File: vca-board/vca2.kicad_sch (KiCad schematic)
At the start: 8 parts, among them U1 SSI2164-Split, U4 TL074

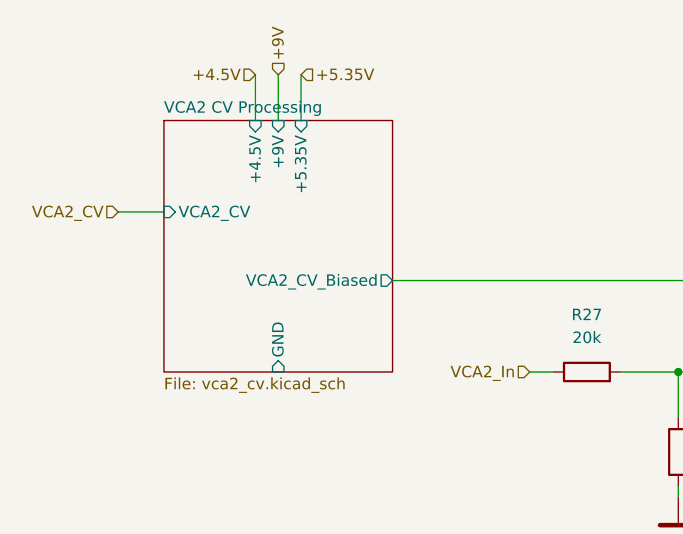
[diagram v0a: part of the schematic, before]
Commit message: VCA components linked
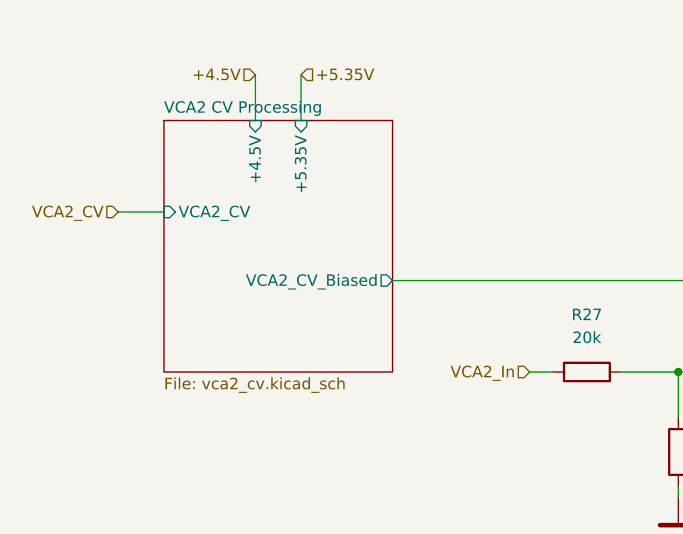
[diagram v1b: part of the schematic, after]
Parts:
- C11: footprint (none) -> Capacitor_SMD:C_0603_1608Metric_Pad1.08x0.95mm_HandSolder; LCSC (none) -> C3012379
- C12: footprint (none) -> Capacitor_SMD:C_0603_1608Metric_Pad1.08x0.95mm_HandSolder; LCSC (none) -> C160903
- R27, R29: LCSC (none) -> C4184
- R28: LCSC (none) -> C22962
- R30: LCSC (none) -> C21190
- U4: footprint (none) -> Package_SO:SOIC-14_3.9x8.7mm_P1.27mm; LCSC (none) -> C6963
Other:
- sheet VCA2 CV Processing ports: added none; removed +9V, GND
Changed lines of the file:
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@@
-    (stroke (width 0) (type default) (color 0 0 0 0))
-  )
-  (wire (pts (xy 63.5 43.18) (xy 63.5 48.26))
     (stroke (width 0) (type default) (color 0 0 0 0))
   )
@@
     (effects (font (size 1.27 1.27)) (justify left))
   )
-  (hierarchical_label "+9V" (shape input) (at 63.5 43.18 90)
-    (effects (font (size 1.27 1.27)) (justify left))
-  )
   (symbol (lib_id "Amplifier_Operational:TL074") (at 146.05 78.74 0) (mirror x) (unit 3)
     (in_bom yes) (on_board yes) (fields_autoplaced)
     (property "Reference" "U4" (id 0) (at 146.05 68.58 0))
     (property "Value" "TL074" (id 1) (at 146.05 71.12 0))
-    (property "Footprint" "" (id 2) (at 144.78 81.28 0)
+    (property "Footprint" "Package_SO:SOIC-14_3.9x8.7mm_P1.27mm" (id 2) (at 144.78 81.28 0)
       (effects (font (size 1.27 1.27)) hide)
     )
     (property "Datasheet" "http://www.ti.com/lit/ds/symlink/tl071.pdf" (id 3) (at 147.32 83.82 0)
+      (effects (font (size 1.27 1.27)) hide)
+    )
+    (property "LCSC" "C6963" (id 4) (at 146.05 78.74 0)
       (effects (font (size 1.27 1.27)) hide)
     )
@@
     (property "Reference" "C12" (id 0) (at 146.05 46.99 90))
     (property "Value" "100p" (id 1) (at 146.05 49.53 90))
-    (property "Footprint" "" (id 2) (at 142.24 55.5752 0)
+    (property "Footprint" "Capacitor_SMD:C_0603_1608Metric_Pad1.08x0.95mm_HandSolder" (id 2) (at 142.24 55.5752 0)
       (effects (font (size 1.27 1.27)) hide)
     )
     (property "Datasheet" "~" (id 3) (at 146.05 54.61 0)
+      (effects (font (size 1.27 1.27)) hide)
+    )
+    (property "LCSC" "C160903" (id 4) (at 146.05 54.61 0)
       (effects (font (size 1.27 1.27)) hide)
     )
@@
     )
     (property "Datasheet" "~" (id 3) (at 97.79 76.2 0)
+      (effects (font (size 1.27 1.27)) hide)
+    )
+    (property "LCSC" "C4184" (id 4) (at 97.79 76.2 0)
       (effects (font (size 1.27 1.27)) hide)
     )
@@
       (effects (font (size 1.27 1.27)) hide)
     )
+    (property "LCSC" "C4184" (id 4) (at 146.05 66.04 0)
+      (effects (font (size 1.27 1.27)) hide)
+    )
     (pin "1")
     (pin "2")
@@
       (effects (font (size 1.27 1.27)) (justify right))
     )
-    (property "Footprint" "" (id 2) (at 106.9848 90.17 0)
+    (property "Footprint" "Capacitor_SMD:C_0603_1608Metric_Pad1.08x0.95mm_HandSolder" (id 2) (at 106.9848 90.17 0)
       (effects (font (size 1.27 1.27)) hide)
     )
     (property "Datasheet" "~" (id 3) (at 107.95 93.98 0)
+      (effects (font (size 1.27 1.27)) hide)
+    )
+    (property "LCSC" "C3012379" (id 4) (at 107.95 93.98 0)
       (effects (font (size 1.27 1.27)) hide)
     )
@@
       (effects (font (size 1.27 1.27)) hide)
     )
+    (property "LCSC" "C21190" (id 4) (at 162.56 78.74 0)
+      (effects (font (size 1.27 1.27)) hide)
+    )
     (pin "1")
     (pin "2")
@@
     )
     (property "Datasheet" "~" (id 3) (at 107.95 85.09 0)
+      (effects (font (size 1.27 1.27)) hide)
+    )
+    (property "LCSC" "C22962" (id 4) (at 107.95 85.09 0)
       (effects (font (size 1.27 1.27)) hide)
     )
@@
       (effects (font (size 1.27 1.27)) (justify left top))
     )
-    (pin "GND" input (at 63.5 76.2 270)
-      (effects (font (size 1.27 1.27)) (justify left))
-    )
-    (pin "+9V" input (at 63.5 48.26 90)
-      (effects (font (size 1.27 1.27)) (justify right))
-    )
     (pin "VCA2_CV" input (at 50.8 58.42 180)

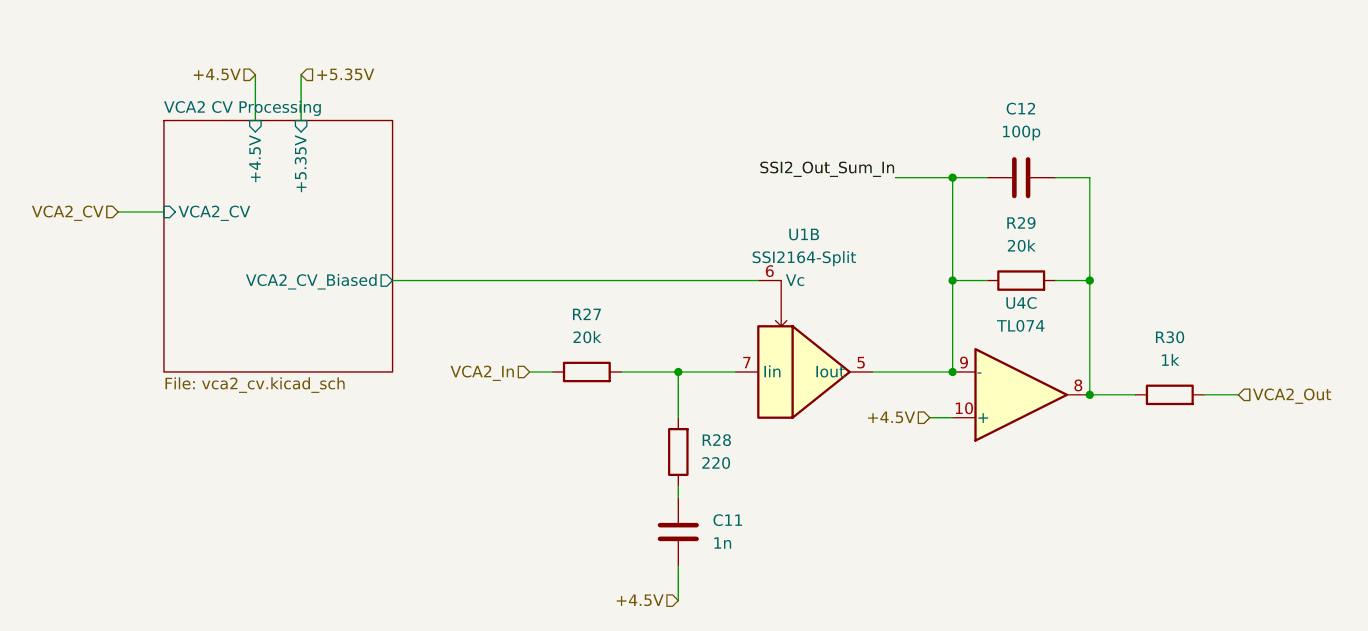
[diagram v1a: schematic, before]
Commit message: VCA board components placed
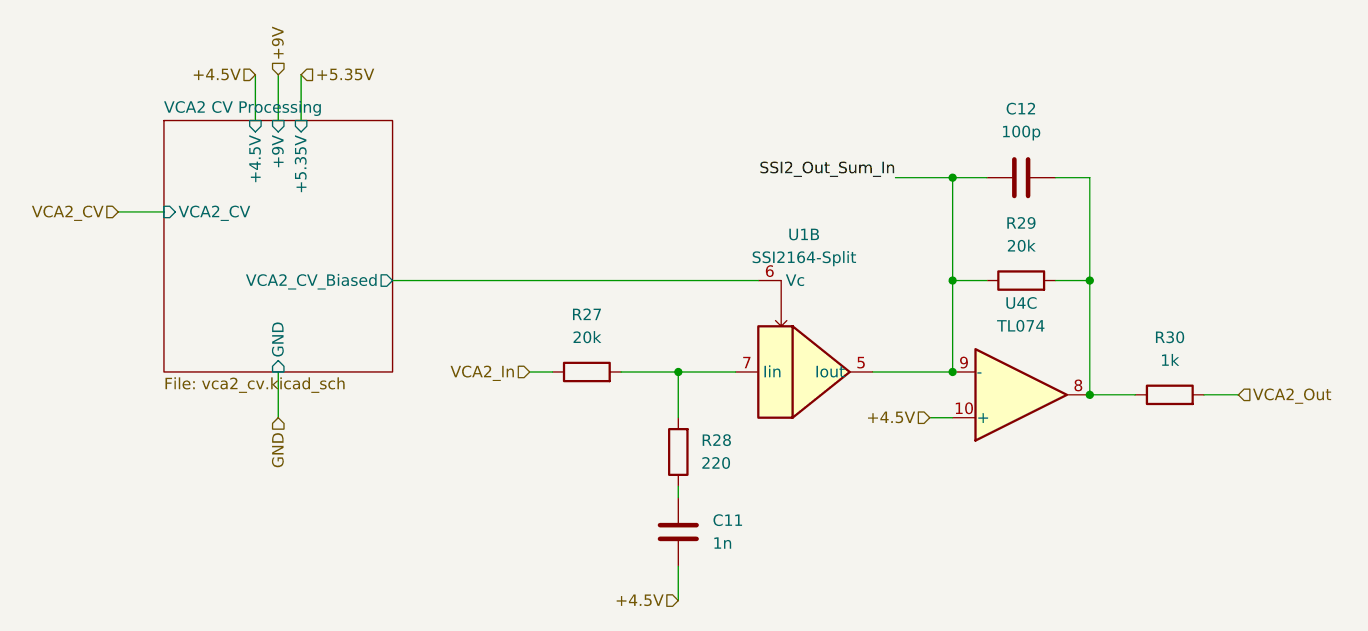
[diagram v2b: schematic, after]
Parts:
- R27, R28, R29, R30: footprint (none) -> Resistor_SMD:R_0603_1608Metric_Pad0.98x0.95mm_HandSolder
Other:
- sheet VCA2 CV Processing ports: added +9V, GND; removed none
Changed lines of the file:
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@@
+    (stroke (width 0) (type default) (color 0 0 0 0))
+  )
+  (wire (pts (xy 63.5 76.2) (xy 63.5 81.28))
     (stroke (width 0) (type default) (color 0 0 0 0))
   )
@@
   )
   (wire (pts (xy 149.86 66.04) (xy 153.67 66.04))
+    (stroke (width 0) (type default) (color 0 0 0 0))
+  )
+  (wire (pts (xy 63.5 43.18) (xy 63.5 48.26))
     (stroke (width 0) (type default) (color 0 0 0 0))
   )
@@
     (effects (font (size 1.27 1.27)) (justify right))
   )
+  (hierarchical_label "+9V" (shape input) (at 63.5 43.18 90)
+    (effects (font (size 1.27 1.27)) (justify left))
+  )
   (hierarchical_label "+4.5V" (shape input) (at 60.96 43.18 180)
     (effects (font (size 1.27 1.27)) (justify right))
@@
   (hierarchical_label "VCA2_Out" (shape input) (at 170.18 78.74 0)
     (effects (font (size 1.27 1.27)) (justify left))
+  )
+  (hierarchical_label "GND" (shape input) (at 63.5 81.28 270)
+    (effects (font (size 1.27 1.27)) (justify right))
   )
   (symbol (lib_id "Amplifier_Operational:TL074") (at 146.05 78.74 0) (mirror x) (unit 3)
@@
     (property "Reference" "R27" (id 0) (at 97.79 69.85 90))
     (property "Value" "20k" (id 1) (at 97.79 72.39 90))
-    (property "Footprint" "" (id 2) (at 97.79 77.978 90)
+    (property "Footprint" "Resistor_SMD:R_0603_1608Metric_Pad0.98x0.95mm_HandSolder" (id 2) (at 97.79 77.978 90)
       (effects (font (size 1.27 1.27)) hide)
     )
@@
     (property "Reference" "R29" (id 0) (at 146.05 59.69 90))
     (property "Value" "20k" (id 1) (at 146.05 62.23 90))
-    (property "Footprint" "" (id 2) (at 146.05 67.818 90)
+    (property "Footprint" "Resistor_SMD:R_0603_1608Metric_Pad0.98x0.95mm_HandSolder" (id 2) (at 146.05 67.818 90)
       (effects (font (size 1.27 1.27)) hide)
     )
@@
     (property "Reference" "R30" (id 0) (at 162.56 72.39 90))
     (property "Value" "1k" (id 1) (at 162.56 74.93 90))
-    (property "Footprint" "" (id 2) (at 162.56 80.518 90)
+    (property "Footprint" "Resistor_SMD:R_0603_1608Metric_Pad0.98x0.95mm_HandSolder" (id 2) (at 162.56 80.518 90)
       (effects (font (size 1.27 1.27)) hide)
     )
@@
       (effects (font (size 1.27 1.27)) (justify right))
     )
-    (property "Footprint" "" (id 2) (at 109.728 85.09 90)
+    (property "Footprint" "Resistor_SMD:R_0603_1608Metric_Pad0.98x0.95mm_HandSolder" (id 2) (at 109.728 85.09 90)
       (effects (font (size 1.27 1.27)) hide)
     )
@@
       (effects (font (size 1.27 1.27)) (justify right))
     )
-  )
+    (pin "+9V" input (at 63.5 48.26 90)
+      (effects (font (size 1.27 1.27)) (justify right))
+    )
+    (pin "GND" input (at 63.5 76.2 270)
+      (effects (font (size 1.27 1.27)) (justify left))
+    )
+  )

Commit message: Filter board schem done
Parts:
- C11: value 1n -> 1.2n; LCSC C3012379 -> C576816
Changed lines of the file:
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@@
       (effects (font (size 1.27 1.27)) (justify right))
     )
-    (property "Value" "1n" (id 1) (at 111.76 95.2499 0)
+    (property "Value" "1.2n" (id 1) (at 111.76 95.2499 0)
       (effects (font (size 1.27 1.27)) (justify right))
     )
@@
       (effects (font (size 1.27 1.27)) hide)
     )
-    (property "LCSC" "C3012379" (id 4) (at 107.95 93.98 0)
+    (property "LCSC" "C576816" (id 4) (at 107.95 93.98 0)
       (effects (font (size 1.27 1.27)) hide)
     )

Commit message: Remove D from linear VCA + update graphics
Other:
- company: (none) -> Pedal Markt / Andrey Salomatin
- title: (none) -> VCA Board
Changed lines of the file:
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@@
 (kicad_sch (version 20211123) (generator eeschema)
   (paper "A4")
+  (title_block
+    (title "VCA Board")
+    (date "2024-11-07")
+    (rev "v1rev2")
+    (company "Pedal Markt / Andrey Salomatin")
+  )
   (junction (at 138.43 66.04) (diameter 0) (color 0 0 0 0)
   )

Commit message: wip pre-redo orientation
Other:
- company: Pedal Markt / Andrey Salomatin -> Andrey Salomatin / Pedal Markt
- title: VCA Board -> Mag
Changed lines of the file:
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@@
   (paper "A4")
   (title_block
-    (title "VCA Board")
+    (title "Mag")
     (date "2024-11-07")
     (rev "v1rev2")
-    (company "Pedal Markt / Andrey Salomatin")
+    (company "Andrey Salomatin / Pedal Markt")
   )
   (junction (at 138.43 66.04) (diameter 0) (color 0 0 0 0)
